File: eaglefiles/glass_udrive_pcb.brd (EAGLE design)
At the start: 14.9 x 20 mm, 31 parts, among them P1 OMNETICS_A75243-001, U1 ANALOG-DEVICES-E14_AD8426ACPZ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

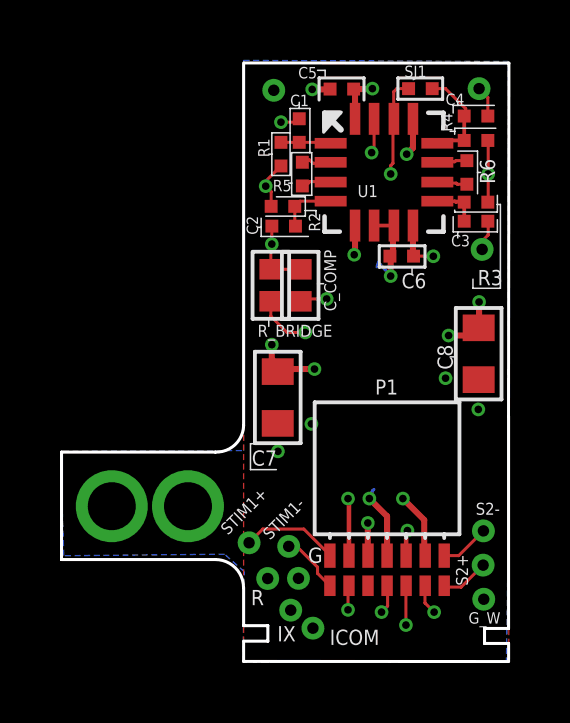
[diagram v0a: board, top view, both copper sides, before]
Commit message: minor routing and dimention and docu layer improvements.
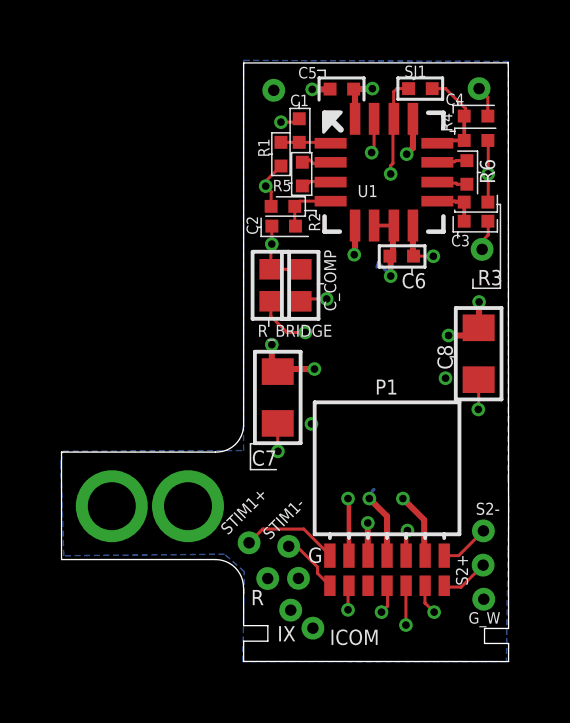
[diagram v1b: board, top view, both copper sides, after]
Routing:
- net GND: track 11.5 -> 13.4 mm
- removed copper zone on layer 1, net GND
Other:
- outline, holes or cut-outs redrawn
